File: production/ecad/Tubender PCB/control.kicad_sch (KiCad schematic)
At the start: 46 parts, among them J1 USB4110GFA, Q1 AO3400A, Q2 AO3400A, U10 MCP23017-E_SO, U2 ESP32-WROOM-32UE_M113EH6400UH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, U3 MCP23017-E_SO, U4 FT232RL-REEL

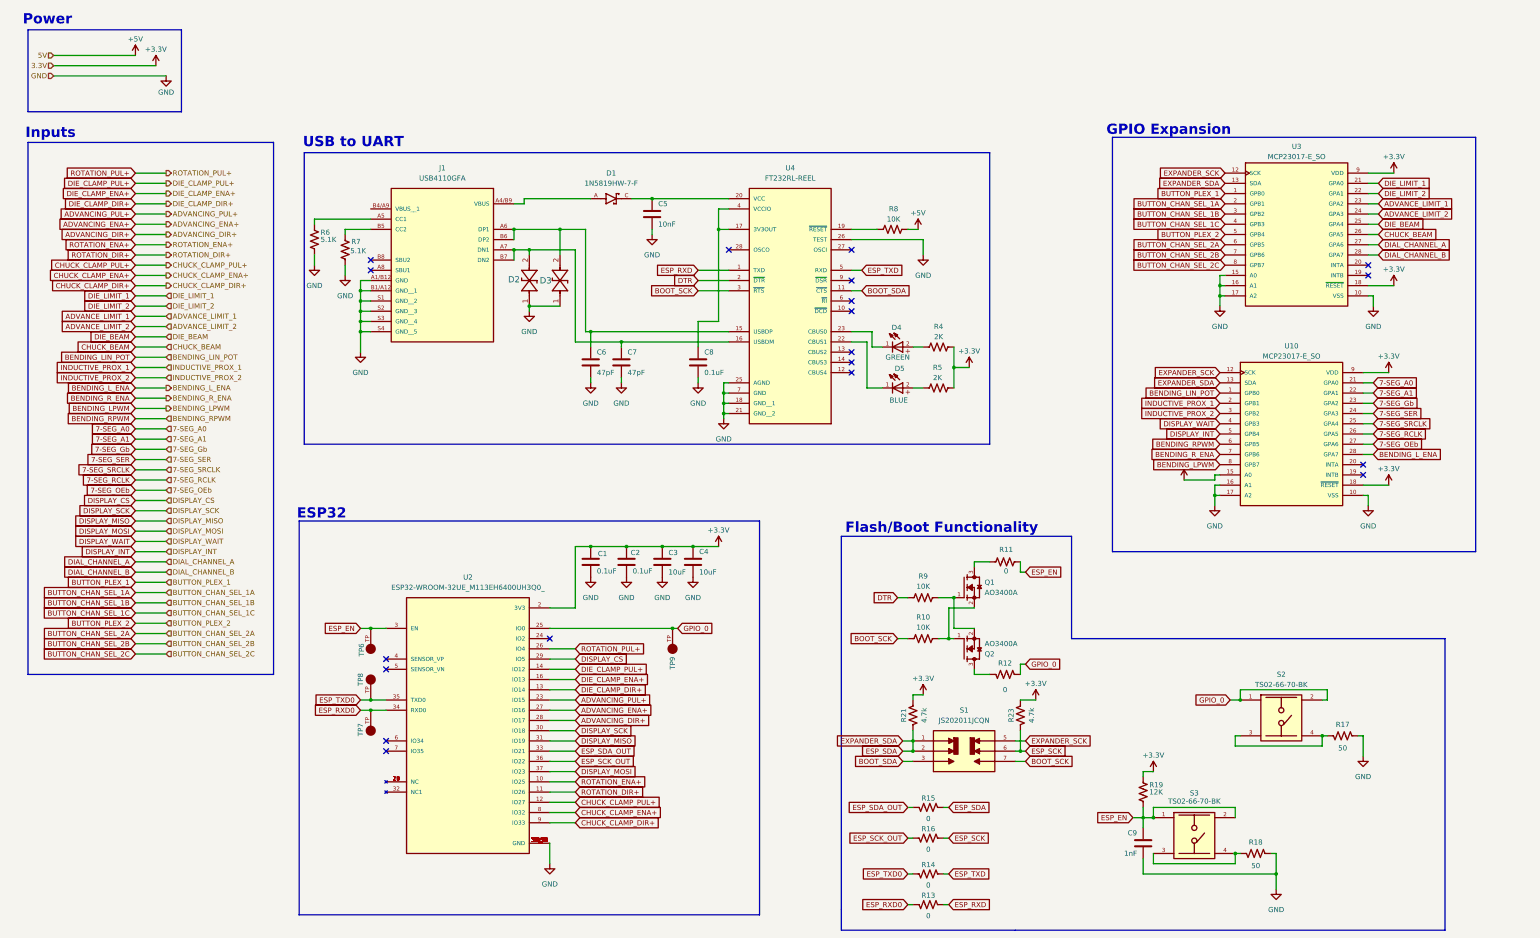
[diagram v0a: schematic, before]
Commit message: Flashing and Buttons
Moved to a more proven way to flash ESP's and also made all the buttons pull ups instead of pull downs.
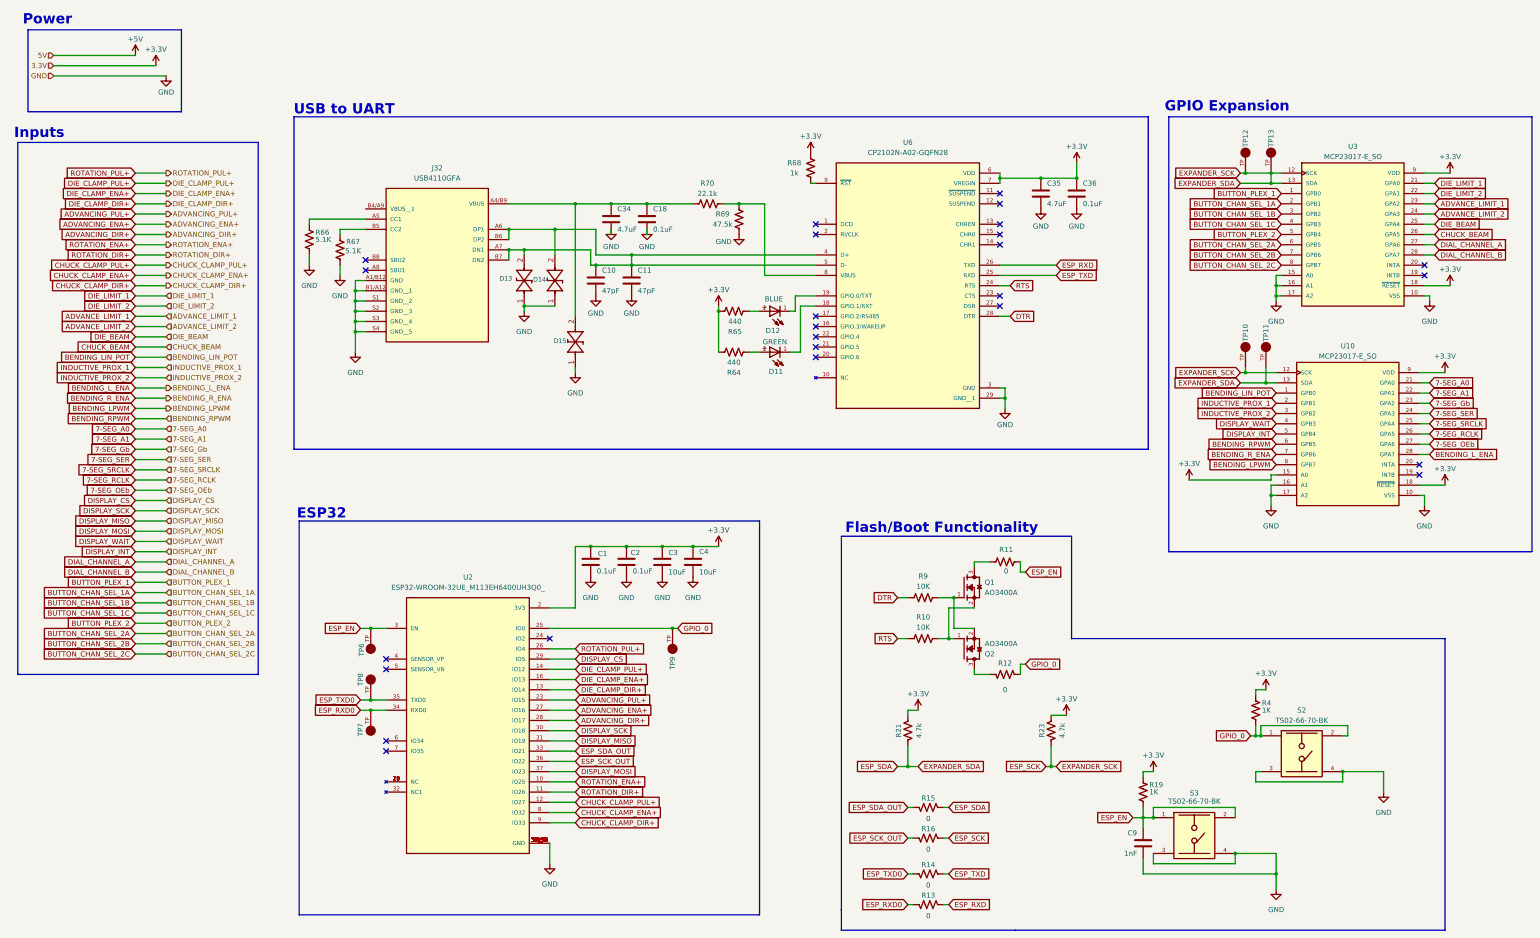
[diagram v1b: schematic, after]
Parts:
- removed C5: 10nF, symbol Device:C
- removed C6, C7: 47pF, symbol Device:C
- removed C8: 0.1uF, symbol Device:C
- removed D1: 1N5819HW-7-F, 1N5819HW-7-F:SOD3715X145N, symbol 1N5819HW-7-F:1N5819HW-7-F
- removed D2, D3: RCLAMP1521P.TCT, TVS_DFN2_SLP1006P2_SEM, symbol RCLAMP1521P:RCLAMP1521P.TCT
- removed D4: GREEN, WL-SMCW_0603:WL-SMCW_0603, symbol WL-SMCW_0603:WL-SMCW_0603
- removed D5: BLUE, WL-SMCW_0603:WL-SMCW_0603, symbol WL-SMCW_0603:WL-SMCW_0603
- removed J1: USB4110GFA, USB4110GFA:GCT_USB4110GFA, symbol USB4110GFA:USB4110GFA
- removed R17, R18: 50, symbol Device:R_US
- removed R5: 2K, symbol Device:R_US
- removed R6, R7: 5.1K, symbol Device:R_US
- removed R8: 10K, symbol Device:R_US
- removed S1: JS202011JCQN, JS202011JCQN:SW_JS202011JCQN, symbol JS202011JCQN:JS202011JCQN
- removed U4: FT232RL-REEL, FT232RL-REEL:SOP65P780X200-28N, symbol FT232RL-REEL:FT232RL-REEL
- added C10, C11: 47pF, symbol Device:C
- added C18, C36: 0.1uF, symbol Device:C
- added C34, C35: 4.7uF, symbol Device:C
- added D11: GREEN, WL-SMCW_0603:WL-SMCW_0603, symbol WL-SMCW_0603:WL-SMCW_0603
- added D12: BLUE, WL-SMCW_0603:WL-SMCW_0603, symbol WL-SMCW_0603:WL-SMCW_0603
- added D13, D14, D15: RCLAMP1521P.TCT, TVS_DFN2_SLP1006P2_SEM, symbol RCLAMP1521P:RCLAMP1521P.TCT
- added J32: USB4110GFA, USB4110GFA:GCT_USB4110GFA, symbol USB4110GFA:USB4110GFA
- added R64, R65: 440, symbol Device:R_US
- added R66, R67: 5.1K, symbol Device:R_US
- added R68: 1k, symbol Device:R_US
- added R69: 47.5k, symbol Device:R_US
- added R70: 22.1k, symbol Device:R_US
- added TP10, TP11, TP12, TP13: 5006, 5006:KEYSTONE_5006, symbol 5006:5006
- added U6: CP2102N-A02-GQFN28, CP2102N-A02-GQFN28:QFN50P500X500X80-29N, symbol CP2102N-A02-GQFN28:CP2102N-A02-GQFN28
- R19: value 12K -> 1K
- R4: value 2K -> 1K
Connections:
- net ESP_SDA is gone; now on net ESP_SCK: R15.2, R21.1, U10.13 (SDA), U3.13 (SDA)
- net EXPANDER_SCK is gone; now on net ESP_SCK: U10.12 (SCK), U3.12 (SCK)
- net +3.3V: now also C35.1, C36.1, R64.2, R65.2, R68.2, U6.6 (VDD), U6.7 (VREGIN)
- net DTR: now also U6.28 (DTR)
- net ESP_RXD: now also U6.26 (TXD)
- net ESP_SCK: now also TP10.TP, TP11.TP, TP12.TP, TP13.TP
- net ESP_TXD: now also U6.25 (RXD)
- net GND: now also S2.3, S2.4, S3.3, S3.4, C10.2, C11.2, C18.2, C34.2, C35.2, C36.2, D13.1, D14.1, D15.1, J32.A1/B12 (GND), J32.B1/A12 (GND__1), J32.S1 (GND__2), J32.S2 (GND__3), J32.S3 (GND__4), J32.S4 (GND__5), R66.1, R67.1, R69.1, U6.29 (GND__1), U6.3 (GND)
- net GPIO_0: now also R4.1
- net BOOT_SCK renamed RTS
- net RTS: now also U6.24 (RTS)
- new net: C18.1, C34.1, D15.2, J32.A4/B9 (VBUS), R70.1
- new net: R68.1, U6.9 (~{RST})
- new net: D12.2, R65.1
- new net: R69.2, R70.2, U6.8 (VBUS)
- new net: D11.2, R64.1
- new net: J32.B5 (CC2), R67.2
- new net: D11.1, U6.18 (GPIO.1/RXT)
- new net: C10.1, C11.1, D13.2, D14.2, J32.A6 (DP1), J32.A7 (DN1), J32.B6 (DP2), J32.B7 (DN2), U6.4 (D+), U6.5 (D-)
- new net: D12.1, U6.19 (GPIO.0/TXT)
- new net: J32.A5 (CC1), R66.2
- no-connect marks 19 -> 25
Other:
- moved on the sheet: R21, R23, S2, U10, U3

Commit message: annotate schematic
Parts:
- renumbered R23 to R_ESP23, R21 to R_ESP33
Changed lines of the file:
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@@
 		(on_board yes)
 		(dnp no)
-		(property "Reference" "R23"
+		(property "Reference" "R_ESP23"
 			(at 269.494 195.58 90)
 			(effects
@@
 			(project "Tubender PCB"
 				(path "/3e1aedd0-6089-4edb-92c7-0c31da2e7927/970b1c80-6c89-48ca-aa97-a5b3735d13b7"
-					(reference "R23")
+					(reference "R_ESP23")
 					(unit 1)
 				)
@@
 		(on_board yes)
 		(dnp no)
-		(property "Reference" "R21"
+		(property "Reference" "R_ESP33"
 			(at 233.934 195.58 90)
 			(effects
@@
 			(project "Tubender PCB"
 				(path "/3e1aedd0-6089-4edb-92c7-0c31da2e7927/970b1c80-6c89-48ca-aa97-a5b3735d13b7"
-					(reference "R21")
+					(reference "R_ESP33")
 					(unit 1)
 				)

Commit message: start power layout
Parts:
- C1, C10, C11, C18, C2, C3, C34, C35, C36, C4, C9: footprint (none) -> Capacitor_SMD:C_0805_2012Metric
- D11, D12: footprint WL-SMCW_0603:WL-SMCW_0603 -> ${KIPRJMOD}:WL-SMCW_0603
- D13, D14, D15: footprint TVS_DFN2_SLP1006P2_SEM -> ${KIPRJMOD}:TVS_DFN2_SLP1006P2_SEM
- J32: footprint USB4110GFA:GCT_USB4110GFA -> ${KIPRJMOD}:GCT_USB4110GFA
- Q1, Q2: footprint AO3400A:SOT95P280X125-3N -> ${KIPRJMOD}:SOT95P280X125-3N
- R10, R11, R12, R13, R14, R15, R16, R19, R4, R64, R65, R66, R67, R68, R69, R70, R9, R_ESP23, R_ESP33: footprint (none) -> Resistor_SMD:R_0805_2012Metric
- S2, S3: footprint TS02-66-70-BK-260-LCR-D:SW_TS02-66-70-BK-260-LCR-D -> ${KIPRJMOD}:SW_TS02-66-70-BK-260-LCR-D
- TP10, TP11, TP12, TP13, TP6, TP7, TP8, TP9: footprint 5006:KEYSTONE_5006 -> ${KIPRJMOD}:KEYSTONE_5006
- U10, U3: footprint MCP23017-E_SO:SOIC127P1030X265-28N -> ${KIPRJMOD}:SOIC127P1030X265-28N
- U2: footprint ESP32-WROOM-32UE_M113EH6400UH3Q0_:MODULE_ESP32-WROOM-32UE_M113EH6400UH3Q0_ -> ${KIPRJMOD}:MODULE_ESP32-WROOM-32UE_M113EH6400UH3Q0_
- U6: footprint CP2102N-A02-GQFN28:QFN50P500X500X80-29N -> ${KIPRJMOD}:QFN50P500X500X80-29N
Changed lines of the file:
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@@
 			)
 		)
-		(property "Footprint" ""
+		(property "Footprint" "Capacitor_SMD:C_0805_2012Metric"
 			(at 163.5252 72.39 0)
 			(effects
@@
 			)
 		)
-		(property "Footprint" "ESP32-WROOM-32UE_M113EH6400UH3Q0_:MODULE_ESP32-WROOM-32UE_M113EH6400UH3Q0_"
+		(property "Footprint" "${KIPRJMOD}:MODULE_ESP32-WROOM-32UE_M113EH6400UH3Q0_"
 			(at 127 195.58 0)
 			(effects
@@
 			)
 		)
-		(property "Footprint" ""
+		(property "Footprint" "Resistor_SMD:R_0805_2012Metric"
 			(at 211.074 55.626 90)
 			(effects
@@
 			)
 		)
-		(property "Footprint" ""
+		(property "Footprint" "Resistor_SMD:R_0805_2012Metric"
 			(at 241.554 232.156 90)
 			(effects
@@
 			)
 		)
-		(property "Footprint" ""
+		(property "Footprint" "Resistor_SMD:R_0805_2012Metric"
 			(at 192.786 92.456 90)
 			(effects
@@
 			)
 		)
-		(property "Footprint" ""
+		(property "Footprint" "Capacitor_SMD:C_0805_2012Metric"
 			(at 270.2052 66.04 0)
 			(effects
@@
 			)
 		)
-		(property "Footprint" "TVS_DFN2_SLP1006P2_SEM"
+		(property "Footprint" "${KIPRJMOD}:TVS_DFN2_SLP1006P2_SEM"
 			(at 153.67 92.71 0)
 			(effects
@@
 			)
 		)
-		(property "Footprint" ""
+		(property "Footprint" "Resistor_SMD:R_0805_2012Metric"
 			(at 193.294 68.326 90)
 			(effects
@@
 			)
 		)
-		(property "Footprint" "AO3400A:SOT95P280X125-3N"
+		(property "Footprint" "${KIPRJMOD}:SOT95P280X125-3N"
 			(at 250.19 160.02 0)
 			(effects
@@
 			)
 		)
-		(property "Footprint" ""
+		(property "Footprint" "Resistor_SMD:R_0805_2012Metric"
 			(at 272.796 195.326 90)
 			(effects
@@
 			)
 		)
-		(property "Footprint" "TS02-66-70-BK-260-LCR-D:SW_TS02-66-70-BK-260-LCR-D"
+		(property "Footprint" "${KIPRJMOD}:SW_TS02-66-70-BK-260-LCR-D"
 			(at 307.34 220.98 0)
 			(effects
@@
 			)
 		)
-		(property "Footprint" ""
+		(property "Footprint" "Capacitor_SMD:C_0805_2012Metric"
 			(at 172.4152 72.39 0)
 			(effects
@@
 			)
 		)
-		(property "Footprint" ""
+		(property "Footprint" "Resistor_SMD:R_0805_2012Metric"
 			(at 321.564 190.246 90)
 			(effects
@@
 			)
 		)
-		(property "Footprint" ""
+		(property "Footprint" "Resistor_SMD:R_0805_2012Metric"
 			(at 186.944 63.754 90)
 			(effects
@@
 			)
 		)
-		(property "Footprint" "5006:KEYSTONE_5006"
+		(property "Footprint" "${KIPRJMOD}:KEYSTONE_5006"
 			(at 326.39 52.07 0)
 			(effects
@@
 			)
 		)
-		(property "Footprint" "5006:KEYSTONE_5006"
+		(property "Footprint" "${KIPRJMOD}:KEYSTONE_5006"
 			(at 102.87 175.26 0)
 			(effects
@@
 			)
 		)
-		(property "Footprint" "5006:KEYSTONE_5006"
+		(property "Footprint" "${KIPRJMOD}:KEYSTONE_5006"
 			(at 102.87 182.88 0)
 			(effects
@@
 			)
 		)
-		(property "Footprint" "AO3400A:SOT95P280X125-3N"
+		(property "Footprint" "${KIPRJMOD}:SOT95P280X125-3N"
 			(at 250.19 175.26 0)
 			(effects
@@
 			)
 		)
-		(property "Footprint" ""
+		(property "Footprint" "Resistor_SMD:R_0805_2012Metric"
 			(at 192.786 102.616 90)
 			(effects
@@
 			)
 		)
-		(property "Footprint" ""
+		(property "Footprint" "Resistor_SMD:R_0805_2012Metric"
 			(at 94.234 75.946 90)
 			(effects
@@
 			)
 		)
-		(property "Footprint" "WL-SMCW_0603:WL-SMCW_0603"
+		(property "Footprint" "${KIPRJMOD}:WL-SMCW_0603"
 			(at 204.47 101.6 0)
 			(effects
@@
 			)
 		)
-		(property "Footprint" "5006:KEYSTONE_5006"
+		(property "Footprint" "${KIPRJMOD}:KEYSTONE_5006"
 			(at 325.12 100.33 0)
 			(effects
@@
 			)
 		)
-		(property "Footprint" ""
+		(property "Footprint" "Capacitor_SMD:C_0805_2012Metric"
 			(at 279.0952 66.04 0)
 			(effects
@@
 			)
 		)
-		(property "Footprint" ""
+		(property "Footprint" "Resistor_SMD:R_0805_2012Metric"
 			(at 260.604 182.626 90)
 			(effects
@@
 			)
 		)
-		(property "Footprint" ""
+		(property "Footprint" "Resistor_SMD:R_0805_2012Metric"
 			(at 260.604 152.654 90)
 			(effects
@@
 			)
 		)
-		(property "Footprint" "TS02-66-70-BK-260-LCR-D:SW_TS02-66-70-BK-260-LCR-D"
+		(property "Footprint" "${KIPRJMOD}:SW_TS02-66-70-BK-260-LCR-D"
 			(at 334.01 200.66 0)
 			(effects
@@
 			)
 		)
-		(property "Footprint" ""
+		(property "Footprint" "Resistor_SMD:R_0805_2012Metric"
 			(at 240.284 171.704 90)
 			(effects
@@
 			)
 		)
-		(property "Footprint" "5006:KEYSTONE_5006"
+		(property "Footprint" "${KIPRJMOD}:KEYSTONE_5006"
 			(at 320.04 100.33 0)
 			(effects
@@
 			)
 		)
-		(property "Footprint" "5006:KEYSTONE_5006"
+		(property "Footprint" "${KIPRJMOD}:KEYSTONE_5006"
 			(at 177.8 175.26 0)
 			(effects
@@
 			)
 		)
-		(property "Footprint" ""
+		(property "Footprint" "Capacitor_SMD:C_0805_2012Metric"
 			(at 176.2252 157.48 0)
 			(effects
@@
 			)
 		)
-		(property "Footprint" ""
+		(property "Footprint" "Capacitor_SMD:C_0805_2012Metric"
 			(at 159.7152 87.63 0)
 			(effects
@@
 			)
 		)
-		(property "Footprint" "TVS_DFN2_SLP1006P2_SEM"
+		(property "Footprint" "${KIPRJMOD}:TVS_DFN2_SLP1006P2_SEM"
 			(at 148.59 77.47 0)
 			(effects
@@
 			)
 		)
-		(property "Footprint" ""
+		(property "Footprint" "Capacitor_SMD:C_0805_2012Metric"
 			(at 293.6748 227.33 0)
 			(effects
@@
 			)
 		)
-		(property "Footprint" "MCP23017-E_SO:SOIC127P1030X265-28N"
+		(property "Footprint" "${KIPRJMOD}:SOIC127P1030X265-28N"
 			(at 345.44 119.38 0)
 			(effects
@@
 			)
 		)
-		(property "Footprint" ""
+		(property "Footprint" "Capacitor_SMD:C_0805_2012Metric"
 			(at 168.6052 87.63 0)
 			(effects
@@
 			)
 		)
-		(property "Footprint" ""
+		(property "Footprint" "Resistor_SMD:R_0805_2012Metric"
 			(at 240.284 161.544 90)
 			(effects
@@
 			)
 		)
-		(property "Footprint" "MCP23017-E_SO:SOIC127P1030X265-28N"
+		(property "Footprint" "${KIPRJMOD}:SOIC127P1030X265-28N"
 			(at 346.71 69.85 0)
 			(effects
@@
 			)
 		)
-		(property "Footprint" "5006:KEYSTONE_5006"
+		(property "Footprint" "${KIPRJMOD}:KEYSTONE_5006"
 			(at 102.87 195.58 0)
 			(effects
@@
 			)
 		)
-		(property "Footprint" ""
+		(property "Footprint" "Resistor_SMD:R_0805_2012Metric"
 			(at 293.624 210.566 90)
 			(effects
@@
 			)
 		)
-		(property "Footprint" ""
+		(property "Footprint" "Resistor_SMD:R_0805_2012Metric"
 			(at 241.554 223.266 90)
 			(effects
@@
 			)
 		)
-		(property "Footprint" ""
+		(property "Footprint" "Resistor_SMD:R_0805_2012Metric"
 			(at 241.554 239.776 90)
 			(effects
@@
 			)
 		)
-		(property "Footprint" ""
+		(property "Footprint" "Capacitor_SMD:C_0805_2012Metric"
 			(at 167.3352 157.48 0)
 			(effects
@@
 			)
 		)
-		(property "Footprint" ""
+		(property "Footprint" "Resistor_SMD:R_0805_2012Metric"
 			(at 237.236 195.326 90)
 			(effects
@@
 			)
 		)
-		(property "Footprint" "CP2102N-A02-GQFN28:QFN50P500X500X80-29N"
+		(property "Footprint" "${KIPRJMOD}:QFN50P500X500X80-29N"
 			(at 236.22 85.09 0)
 			(effects
@@
 			)
 		)
-		(property "Footprint" ""
+		(property "Footprint" "Resistor_SMD:R_0805_2012Metric"
 			(at 86.614 73.406 90)
 			(effects
@@
 			)
 		)
-		(property "Footprint" "5006:KEYSTONE_5006"
+		(property "Footprint" "${KIPRJMOD}:KEYSTONE_5006"
 			(at 320.04 52.07 0)
 			(effects
@@
 			)
 		)
-		(property "Footprint" "TVS_DFN2_SLP1006P2_SEM"
+		(property "Footprint" "${KIPRJMOD}:TVS_DFN2_SLP1006P2_SEM"
 			(at 140.97 77.47 0)
 			(effects
@@
 			)
 		)
-		(property "Footprint" ""
+		(property "Footprint" "Capacitor_SMD:C_0805_2012Metric"
 			(at 183.8452 157.48 0)
 			(effects
@@
 			)
 		)
-		(property "Footprint" ""
+		(property "Footprint" "Resistor_SMD:R_0805_2012Metric"
 			(at 241.554 215.646 90)
 			(effects
@@
 			)
 		)
-		(property "Footprint" ""
+		(property "Footprint" "Capacitor_SMD:C_0805_2012Metric"
 			(at 158.4452 157.48 0)
 			(effects
@@
 			)
 		)
-		(property "Footprint" "USB4110GFA:GCT_USB4110GFA"
+		(property "Footprint" "${KIPRJMOD}:GCT_USB4110GFA"
 			(at 119.38 71.12 0)
 			(effects
@@
 			)
 		)
-		(property "Footprint" "WL-SMCW_0603:WL-SMCW_0603"
+		(property "Footprint" "${KIPRJMOD}:WL-SMCW_0603"
 			(at 204.47 91.44 0)
 			(effects
